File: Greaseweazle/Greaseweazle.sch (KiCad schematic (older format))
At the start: 19 parts, among them J1 FDC_PC, J2 PWR_EXT1, J3 PWR_DRV, J4 PWR_EXT2, J5 USB_TTL, J6 FDC_Amstrad, M1 Mounting, M2 Mounting, M3 Mounting, M4 Mounting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

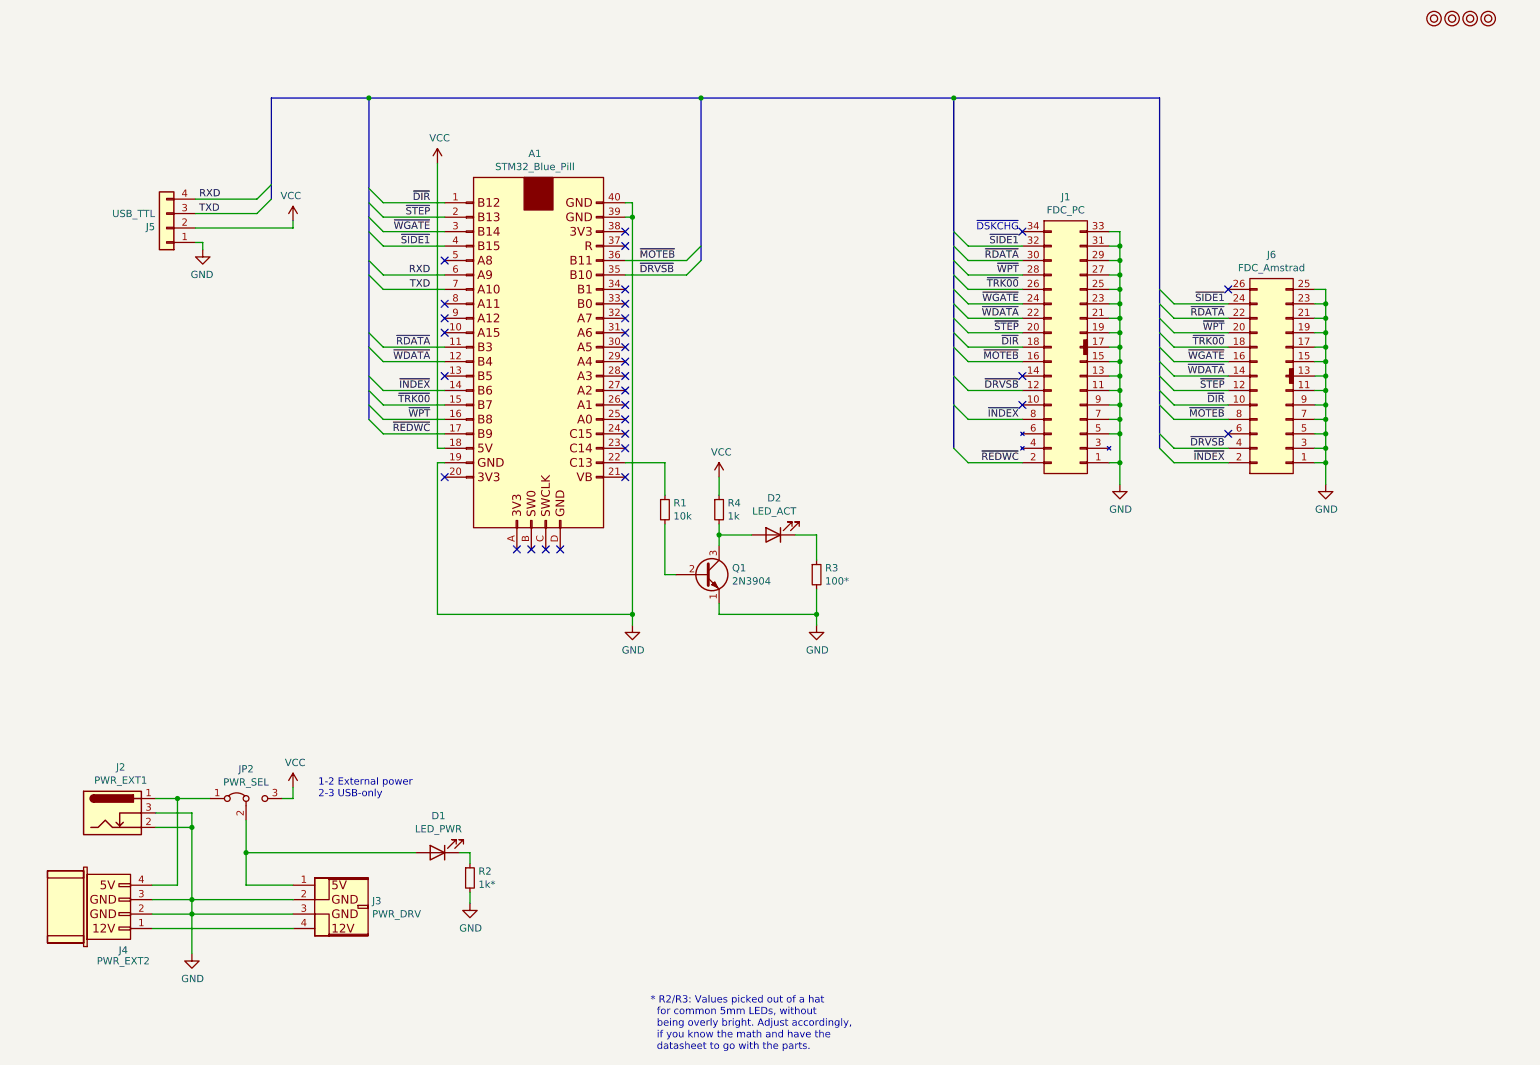
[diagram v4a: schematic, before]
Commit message: Added pullups
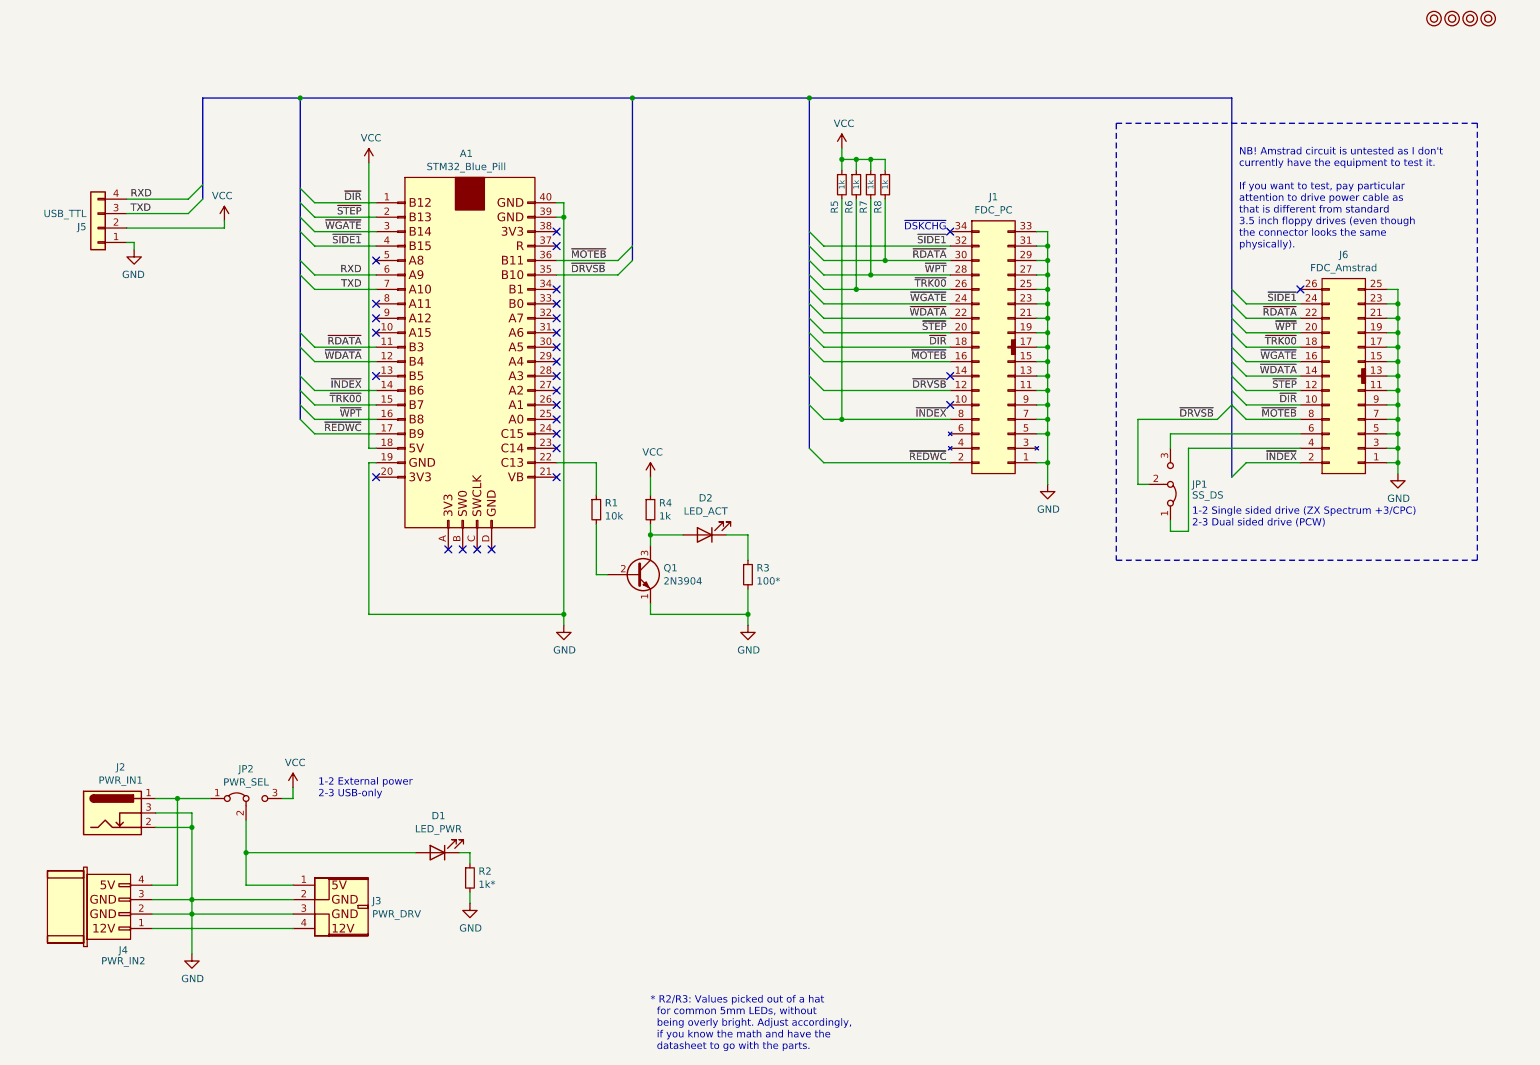
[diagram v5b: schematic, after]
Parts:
- added JP1: SS_DS, Connector_PinHeader_2.54mm:PinHeader_1x03_P2.54mm_Vertical, symbol Jumper:Jumper_3_Bridged12
- added R5, R6, R7, R8: 1k, Resistor_THT:R_Axial_DIN0207_L6.3mm_D2.5mm_P10.16mm_Horizontal, symbol Device:R_Small
- J2: value PWR_EXT1 -> PWR_IN1
- J4: value PWR_EXT2 -> PWR_IN2
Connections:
- net VCC: now also R5.1, R6.1, R7.1, R8.1
- net ~DRVSB: now also JP1.2 (C); no longer J6.4 (nc)
- net ~INDEX: now also R5.2
- net ~RDATA: now also R8.2
- net ~TRK00: now also R6.2
- net ~WPT: now also R7.2
- net at J6.6 (nc): now also JP1.3 (B)
- new net: J6.4 (nc), JP1.1 (A)
- no-connect marks 30 -> 29
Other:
- note added: "1-2 Single sided drive (ZX Spectrum +3/CPC)\n2-3 Dual sided drive (PCW)"
- note added: "NB! Amstrad circuit is untested as I don't\ncurrently have the equipment to test it.\n\nIf you want to test, pay particular\nattention to drive power cable as\nthat is different from standard\n3.5 inch floppy drives (even though\nthe connector looks the same\nphysically)."
- moved on the sheet: A1, D2, J1, J5, J6, Q1, R1, R3, R4

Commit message: Add R10 (in case it is needed)
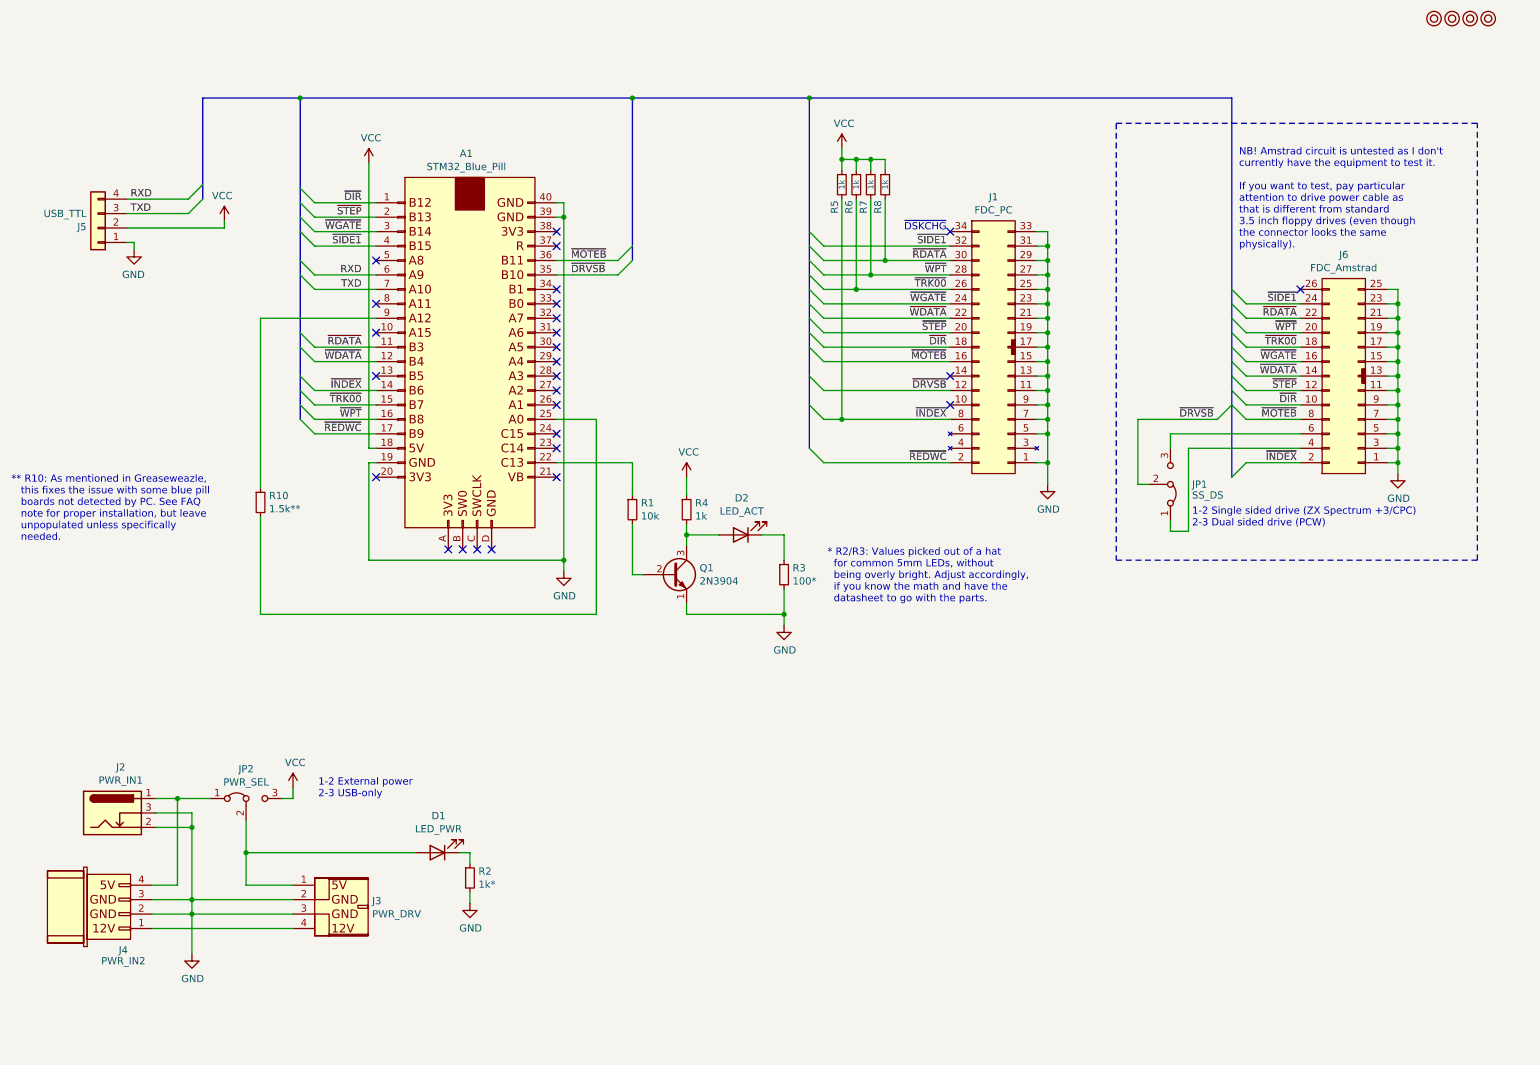
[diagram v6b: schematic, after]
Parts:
- added R10: 1.5k**, Resistor_THT:R_Axial_DIN0207_L6.3mm_D2.5mm_P10.16mm_Horizontal, symbol Device:R_Small
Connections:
- net at A1.25 (A0): now also R10.2
- net at A1.9 (A12): now also R10.1
- no-connect marks 29 -> 27
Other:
- note added: "** R10: As mentioned in Greaseweazle,\n this fixes the issue with some blue pill\n boards not detected by PC. See FAQ\n note for proper installation, but leave\n unpopulated unless specifically\n needed."
- moved on the sheet: D2, Q1, R1, R3, R4
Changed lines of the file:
@@
 L Device:LED D2
 U 1 1 6169A431
-P 5700 4150
-F 0 "D2" H 5693 3895 50  0000 C CNN
-F 1 "LED_ACT" H 5693 3986 50  0000 C CNN
-F 2 "LED_THT:LED_D5.0mm" H 5700 4150 50  0001 C CNN
-F 3 "~" H 5700 4150 50  0001 C CNN
-	1    5700 4150
+P 5950 4150
+F 0 "D2" H 5943 3895 50  0000 C CNN
+F 1 "LED_ACT" H 5943 3986 50  0000 C CNN
+F 2 "LED_THT:LED_D5.0mm" H 5950 4150 50  0001 C CNN
+F 3 "~" H 5950 4150 50  0001 C CNN
+	1    5950 4150
 	-1   0    0    1
 $EndComp
@@
 L Device:R_Small R3
 U 1 1 6169A437
-P 6000 4425
-F 0 "R3" H 6059 4471 50  0000 L CNN
-F 1 "100*" H 6059 4380 50  0000 L CNN
-F 2 "Resistor_THT:R_Axial_DIN0207_L6.3mm_D2.5mm_P10.16mm_Horizontal" H 6000 4425 50  0001 C CNN
-F 3 "~" H 6000 4425 50  0001 C CNN
-	1    6000 4425
+P 6250 4425
+F 0 "R3" H 6309 4471 50  0000 L CNN
+F 1 "100*" H 6309 4380 50  0000 L CNN
+F 2 "Resistor_THT:R_Axial_DIN0207_L6.3mm_D2.5mm_P10.16mm_Horizontal" H 6250 4425 50  0001 C CNN
+F 3 "~" H 6250 4425 50  0001 C CNN
+	1    6250 4425
 	1    0    0    -1
 $EndComp
@@
 NoConn ~ 3425 2250
 NoConn ~ 3425 2550
-NoConn ~ 3425 2650
 NoConn ~ 3425 2750
 NoConn ~ 3425 3050
@@
 NoConn ~ 4675 3550
 NoConn ~ 4675 3450
-NoConn ~ 4675 3350
 NoConn ~ 4675 3250
 NoConn ~ 4675 3150
@@
 L Transistor_BJT:2N3904 Q1
 U 1 1 618EF1F0
-P 5225 4425
-F 0 "Q1" H 5415 4471 50  0000 L CNN
-F 1 "2N3904" H 5415 4380 50  0000 L CNN
-F 2 "Package_TO_SOT_THT:TO-92_Inline_Wide" H 5425 4350 50  0001 L CIN
-F 3 "https://www.onsemi.com/pub/Collateral/2N3903-D.PDF" H 5225 4425 50  0001 L CNN
-	1    5225 4425
+P 5475 4425
+F 0 "Q1" H 5665 4471 50  0000 L CNN
+F 1 "2N3904" H 5665 4380 50  0000 L CNN
+F 2 "Package_TO_SOT_THT:TO-92_Inline_Wide" H 5675 4350 50  0001 L CIN
+F 3 "https://www.onsemi.com/pub/Collateral/2N3903-D.PDF" H 5475 4425 50  0001 L CNN
+	1    5475 4425
 	1    0    0    -1
 $EndComp
@@
 L Device:R_Small R1
 U 1 1 619034E5
-P 4950 3975
-F 0 "R1" H 5009 4021 50  0000 L CNN
-F 1 "10k" H 5009 3930 50  0000 L CNN
-F 2 "Resistor_THT:R_Axial_DIN0207_L6.3mm_D2.5mm_P10.16mm_Horizontal" H 4950 3975 50  0001 C CNN
-F 3 "~" H 4950 3975 50  0001 C CNN
-	1    4950 3975
-	1    0    0    -1
-$EndComp
-Wire Wire Line
-	4950 3875 4950 3650
-Wire Wire Line
-	4675 3650 4950 3650
+P 5200 3975
+F 0 "R1" H 5259 4021 50  0000 L CNN
+F 1 "10k" H 5259 3930 50  0000 L CNN
+F 2 "Resistor_THT:R_Axial_DIN0207_L6.3mm_D2.5mm_P10.16mm_Horizontal" H 5200 3975 50  0001 C CNN
+F 3 "~" H 5200 3975 50  0001 C CNN
+	1    5200 3975
+	1    0    0    -1
+$EndComp
+Wire Wire Line
+	5200 3875 5200 3650
 $Comp
 L Device:R_Small R4
 U 1 1 61922ADD
-P 5325 3975
-F 0 "R4" H 5384 4021 50  0000 L CNN
-F 1 "1k" H 5384 3930 50  0000 L CNN
-F 2 "Resistor_THT:R_Axial_DIN0207_L6.3mm_D2.5mm_P10.16mm_Horizontal" H 5325 3975 50  0001 C CNN
-F 3 "~" H 5325 3975 50  0001 C CNN
-	1    5325 3975
-	1    0    0    -1
-$EndComp
-Wire Wire Line
-	4950 4425 5025 4425
-Wire Wire Line
-	4950 4075 4950 4425
-Wire Wire Line
-	5325 4225 5325 4150
-Wire Wire Line
-	5325 4150 5550 4150
-Connection ~ 5325 4150
-Wire Wire Line
-	5325 4150 5325 4075
-Wire Wire Line
-	5325 4625 5325 4700
-Connection ~ 4725 4700
-Wire Wire Line
-	4725 4700 3375 4700
-Wire Wire Line
-	3375 3650 3375 4700
-Wire Wire Line
-	4725 1950 4725 4700
-Wire Wire Line
-	4725 4700 4725 4775
+P 5575 3975
+F 0 "R4" H 5634 4021 50  0000 L CNN
+F 1 "1k" H 5634 3930 50  0000 L CNN
+F 2 "Resistor_THT:R_Axial_DIN0207_L6.3mm_D2.5mm_P10.16mm_Horizontal" H 5575 3975 50  0001 C CNN
+F 3 "~" H 5575 3975 50  0001 C CNN
+	1    5575 3975
+	1    0    0    -1
+$EndComp
+Wire Wire Line
+	5200 4425 5275 4425
+Wire Wire Line
+	5200 4075 5200 4425
+Wire Wire Line
+	5575 4225 5575 4150
+Wire Wire Line
+	5575 4150 5800 4150
+Connection ~ 5575 4150
+Wire Wire Line
+	5575 4150 5575 4075
+Wire Wire Line
+	5575 4625 5575 4700
+Wire Wire Line
+	3375 3650 3375 4325
+Wire Wire Line
+	4725 1950 4725 4325
 $Comp
 L power:GND #PWR0102
 U 1 1 6196B6B9
-P 4725 4775
-F 0 "#PWR0102" H 4725 4525 50  0001 C CNN
-F 1 "GND" H 4730 4602 50  0000 C CNN
-F 2 "" H 4725 4775 50  0001 C CNN
-F 3 "" H 4725 4775 50  0001 C CNN
-	1    4725 4775
+P 4725 4400
+F 0 "#PWR0102" H 4725 4150 50  0001 C CNN
+F 1 "GND" H 4730 4227 50  0000 C CNN
+F 2 "" H 4725 4400 50  0001 C CNN
+F 3 "" H 4725 4400 50  0001 C CNN
+	1    4725 4400
 	1    0    0    -1
 $EndComp
@@
 L power:VCC #PWR02
 U 1 1 619B0A7B
-P 5325 3750
-F 0 "#PWR02" H 5325 3600 50  0001 C CNN
-F 1 "VCC" H 5340 3923 50  0000 C CNN
-F 2 "" H 5325 3750 50  0001 C CNN
-F 3 "" H 5325 3750 50  0001 C CNN
-	1    5325 3750
-	1    0    0    -1
-$EndComp
-Wire Wire Line
-	5325 3750 5325 3875
-Wire Wire Line
-	6000 4150 6000 4325
-Wire Wire Line
-	5850 4150 6000 4150
-Wire Wire Line
-	5325 4700 6000 4700
+P 5575 3750
+F 0 "#PWR02" H 5575 3600 50  0001 C CNN
+F 1 "VCC" H 5590 3923 50  0000 C CNN
+F 2 "" H 5575 3750 50  0001 C CNN
+F 3 "" H 5575 3750 50  0001 C CNN
+	1    5575 3750
+	1    0    0    -1
+$EndComp
+Wire Wire Line
+	5575 3750 5575 3875
+Wire Wire Line
+	6250 4150 6250 4325
+Wire Wire Line
+	6100 4150 6250 4150
+Wire Wire Line
+	5575 4700 6250 4700
 $Comp
 L power:GND #PWR03
 U 1 1 61A2D4B6
-P 6000 4775
-F 0 "#PWR03" H 6000 4525 50  0001 C CNN
-F 1 "GND" H 6005 4602 50  0000 C CNN
-F 2 "" H 6000 4775 50  0001 C CNN
-F 3 "" H 6000 4775 50  0001 C CNN
-	1    6000 4775
-	1    0    0    -1
-$EndComp
-Wire Wire Line
-	6000 4525 6000 4700
-Connection ~ 6000 4700
-Wire Wire Line
-	6000 4700 6000 4775
-Text Notes 5325 7725 0    50   ~ 0
+P 6250 4775
+F 0 "#PWR03" H 6250 4525 50  0001 C CNN
+F 1 "GND" H 6255 4602 50  0000 C CNN
+F 2 "" H 6250 4775 50  0001 C CNN
+F 3 "" H 6250 4775 50  0001 C CNN
+	1    6250 4775
+	1    0    0    -1
+$EndComp
+Wire Wire Line
+	6250 4525 6250 4700
+Connection ~ 6250 4700
+Wire Wire Line
+	6250 4700 6250 4775
+Text Notes 6550 4625 0    50   ~ 0
 * R2/R3: Values picked out of a hat\n  for common 5mm LEDs, without\n  being overly bright. Adjust accordingly,\n  if you know the math and have the\n  datasheet to go with the parts.
 NoConn ~ 7400 3050
@@
 	1    0    0    -1
 $EndComp
+Wire Wire Line
+	3375 4325 4725 4325
+Wire Wire Line
+	4725 4325 4725 4400
+Connection ~ 4725 4325
+Wire Wire Line
+	4675 3650 5200 3650
+Wire Wire Line
+	4675 3350 4950 3350
+Wire Wire Line
+	4950 3350 4950 4700
+Wire Wire Line
+	2625 2650 3425 2650
+$Comp
+L Device:R_Small R10
+U 1 1 61A6357B
+P 2625 3925
+F 0 "R10" H 2684 3971 50  0000 L CNN
+F 1 "1.5k**" H 2684 3880 50  0000 L CNN
+F 2 "Resistor_THT:R_Axial_DIN0207_L6.3mm_D2.5mm_P10.16mm_Horizontal" H 2625 3925 50  0001 C CNN
+F 3 "~" H 2625 3925 50  0001 C CNN
+	1    2625 3925
+	1    0    0    -1
+$EndComp
+Wire Wire Line
+	2625 2650 2625 3825
+Wire Wire Line
+	2625 4025 2625 4700
+Wire Wire Line
+	2625 4700 4950 4700
+Text Notes 900  4200 0    50   ~ 0
+** R10: As mentioned in Greaseweazle,\n   this fixes the issue with some blue pill\n   boards not detected by PC. See FAQ\n   note for proper installation, but leave\n   unpopulated unless specifically\n   needed.
 Wire Bus Line
 	2225 1125 2225 1825
